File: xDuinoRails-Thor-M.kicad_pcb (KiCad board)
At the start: 6 copper layers, 30 x 20.1 mm, 38 parts, among them J701 Conn_02x11_Odd_Even, Q501 S8050, Q601 S8550, Q602 S8550, Q604 S8050, Q901 BSS138, Q902 BSS138, U1101 MOUDLE-SEEEDUINO-XIAO, U201 HT75xx-1-SOT89, U801 BDR6133

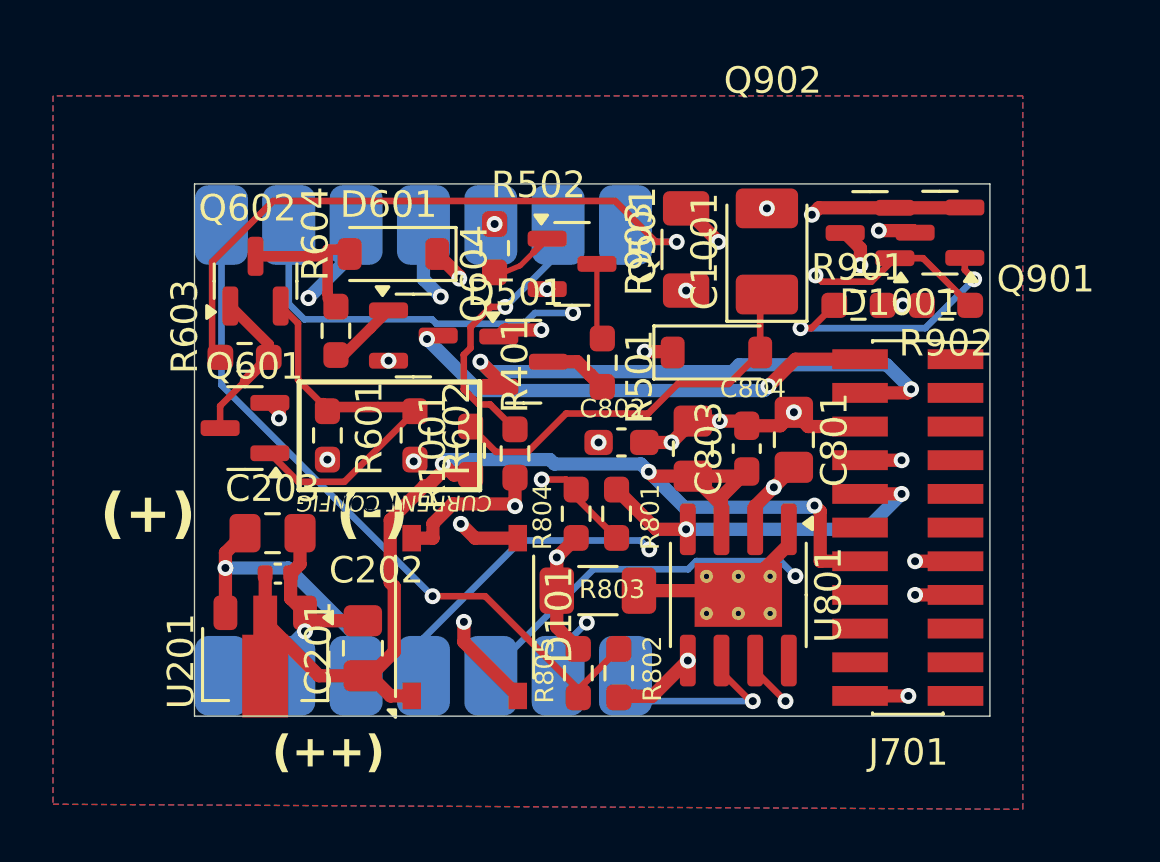
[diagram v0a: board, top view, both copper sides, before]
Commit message: Chg - Clearer PCB layout
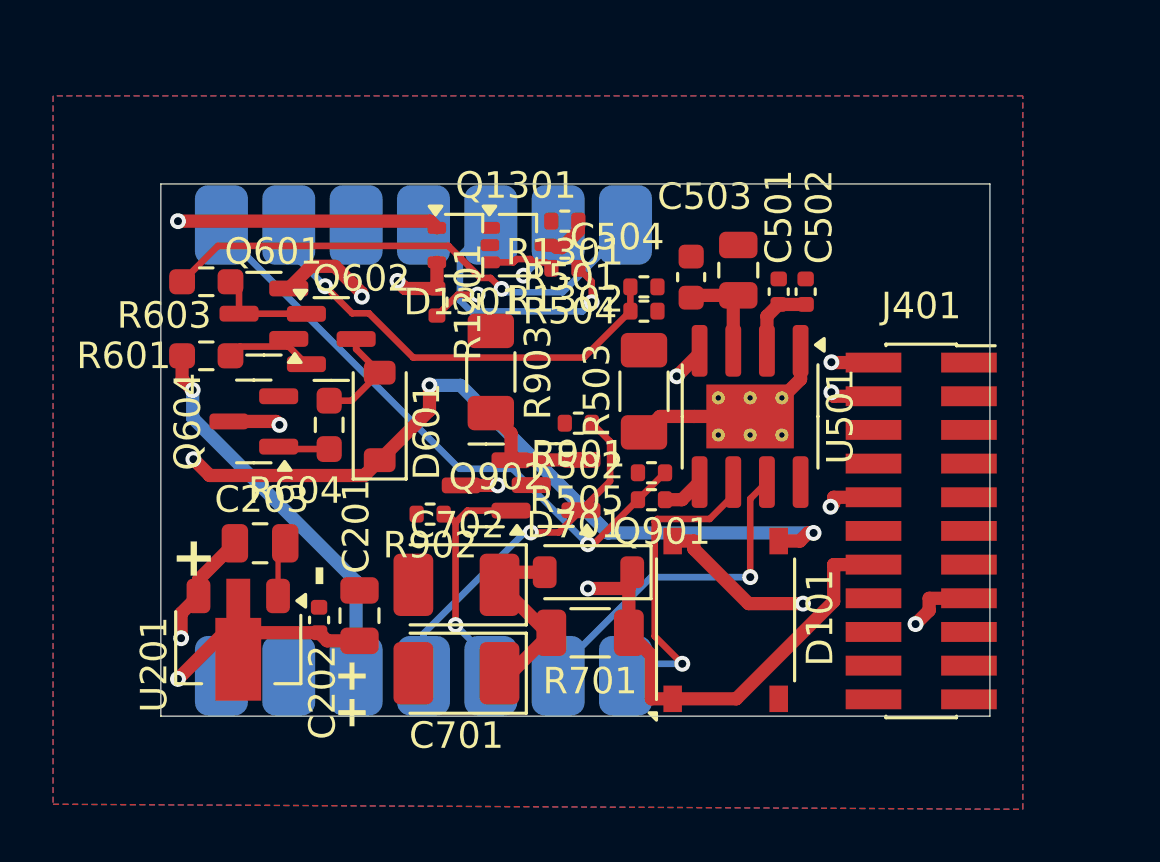
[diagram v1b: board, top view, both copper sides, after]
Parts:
- removed C1001: 100uF, Capacitor_Tantalum_SMD:CP_EIA-3528-21_Kemet-B_Pad1.50x2.35mm_HandSolder
- removed C801, C804: 100nF, Capacitor_SMD:C_0805_2012Metric_Pad1.18x1.45mm_HandSolder
- removed C802, C803: 10uF, Capacitor_SMD:C_0603_1608Metric_Pad1.08x0.95mm_HandSolder
- removed D1001: 1N5819W, Diode_SMD:D_SOD-123
- removed D501: BAT54C, xDuinoRail:8x50_SOT-23
- removed J701: Conn_02x11_Odd_Even, Connector_PinSocket_1.27mm:PinSocket_2x11_P1.27mm_Vertical_SMD
- removed Q501: S8050, xDuinoRail:8x50_SOT-23
- removed R1001: 100R, Resistor_SMD:R_0603_1608Metric_Pad0.98x0.95mm_HandSolder
- removed R401: 33k, Resistor_SMD:R_0603_1608Metric_Pad0.98x0.95mm_HandSolder
- removed R602: 1M, Resistor_SMD:R_0603_1608Metric_Pad0.98x0.95mm_HandSolder
- removed R801, R802: 6k8, Resistor_SMD:R_0603_1608Metric_Pad0.98x0.95mm_HandSolder
- removed R803: 0R1, Resistor_SMD:R_1206_3216Metric_Pad1.30x1.75mm_HandSolder
- removed R804, R805: 1k, Resistor_SMD:R_0603_1608Metric_Pad0.98x0.95mm_HandSolder
- removed U801: BDR6133, Package_SO:SOIC-8-1EP_3.9x4.9mm_P1.27mm_EP2.41x3.3mm_ThermalVias
- added C501: 100nF, Capacitor_SMD:C_0402_1005Metric, F.Cu at (165.0, 93.5)
- added C502: 10uF, Capacitor_SMD:C_0402_1005Metric, F.Cu at (166.1, 93.5)
- added C503: 10uF, Capacitor_SMD:C_0805_2012Metric, F.Cu at (163.5, 92.7)
- added C504: 100nF, Capacitor_SMD:C_0603_1608Metric, F.Cu at (161.7, 92.9)
- added C701: 100uF, Capacitor_Tantalum_SMD:CP_EIA-3528-21_Kemet-B_Pad1.50x2.35mm_HandSolder, F.Cu at (152.9, 107.9)
- added C702: 100uF, Capacitor_Tantalum_SMD:CP_EIA-3528-21_Kemet-B_Pad1.50x2.35mm_HandSolder, F.Cu at (152.9, 104.5)
- added D1301: BAT54CW, Package_TO_SOT_SMD:SOT-323_SC-70, F.Cu at (153.1, 91.7)
- added D701: 1N5819W, Diode_SMD:D_SOD-123, F.Cu at (157.9, 104.0)
- added J401: Conn_02x11_Odd_Even, Connector_PinSocket_1.27mm:PinSocket_2x11_P1.27mm_Vertical_SMD, F.Cu at (170.4, 102.5)
- added Q1301: BSS138W, Package_TO_SOT_SMD:SOT-323_SC-70, F.Cu at (155.2, 91.7)
- added R1201: 33k, Resistor_SMD:R_0402_1005Metric, F.Cu at (152.1, 93.9)
- added R1301: 100R, Resistor_SMD:R_0402_1005Metric, F.Cu at (157.0, 90.8)
- added R1302: 10k, Resistor_SMD:R_0402_1005Metric, F.Cu at (157.0, 92.6)
- added R503: 0R1, Resistor_SMD:R_1206_3216Metric_Pad1.30x1.75mm_HandSolder, F.Cu at (160.0, 97.2)
- added R504: 1k, Resistor_SMD:R_0402_1005Metric, F.Cu at (160.0, 94.2)
- added R505: 1k, Resistor_SMD:R_0402_1005Metric, F.Cu at (160.2, 100.3)
- added R701: 100R, Resistor_SMD:R_1206_3216Metric, F.Cu at (157.9, 106.3)
- added U501: BDR6133, Package_SO:SOIC-8-1EP_3.9x4.9mm_P1.27mm_EP2.41x3.3mm_ThermalVias, F.Cu at (164.0, 98.2)
- C201, C203: footprint Capacitor_SMD:C_0805_2012Metric_Pad1.18x1.45mm_HandSolder -> Capacitor_SMD:C_0805_2012Metric
- R501: value 100R -> 6k8; footprint Resistor_SMD:R_0603_1608Metric_Pad0.98x0.95mm_HandSolder -> Resistor_SMD:R_0402_1005Metric
- R502: value 10k -> 6k8; footprint Resistor_SMD:R_0603_1608Metric_Pad0.98x0.95mm_HandSolder -> Resistor_SMD:R_0402_1005Metric
- R901, R902: footprint Resistor_SMD:R_0603_1608Metric_Pad0.98x0.95mm_HandSolder -> Resistor_SMD:R_0402_1005Metric
- moved R902 21.0 mm to (151.9, 101.9)
- moved Q902 17.3 mm to (154.0, 100.8)
- moved Q901 17.3 mm to (156.6, 100.8)
- moved R901 11.5 mm to (157.5, 98.4), turned to 180 degrees
- moved R502 11.2 mm to (160.2, 101.3), turned to 0 degrees
- moved D101 9.84 mm to (163.0, 105.8)
- moved R903 8.70 mm to (154.2, 96.5), turned to -90 degrees
- moved Q604 6.83 mm to (145.2, 98.4), turned to 180 degrees
- moved D601 6.15 mm to (150.0, 98.2), turned to 90 degrees
- moved R601 5.47 mm to (143.4, 95.9), turned to 180 degrees
- moved Q601 4.37 mm to (145.6, 94.3)
- moved Q602 3.59 mm to (148.2, 95.2), turned to 0 degrees
- moved R604 3.56 mm to (148.1, 98.5)
- moved R501 3.26 mm to (160.0, 93.3), turned to 0 degrees
- moved R603 3.20 mm to (143.4, 93.1)
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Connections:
- R501 pad 1: /rails_signal_combined-medium/rails-signal-acknowledge_dcc/DCC+_DROP -> /EMF_MOTOR0
- R501 pad 2: /rails_signal_combined-medium/rails-signal-acknowledge_dcc/DCC+ -> /AMP_MOTOR0
- R502 pad 1: /DCC_ACK -> /EMF_MOTOR1
- R502 pad 2: /rails_signal_combined-medium/rails-signal-acknowledge_dcc/DCC_ACK_IN -> /AMP_MOTOR1
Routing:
- net GND: track 27.2 -> 1.71 mm, vias 11 -> 0
- net /FUNC1: track 32.8 -> 9.19 mm, vias 2 -> 1
- net PGND: track 36.0 -> 13.9 mm, vias 1 -> 0
- net /I_FUNC: track 26.6 -> 4.73 mm, vias 3 -> 0
- net /AMP_MOTOR1: track 21.5 -> 1.58 mm, vias 2 -> 0
- net /FUNC0: track 32.2 -> 13.5 mm, vias 3 -> 1
- net /AMP_FUNC0: track 16.0 -> 0.00 mm, vias 2 -> 0
- net /DCC0: track 40.7 -> 56.4 mm, vias 4 -> 5
- net Net-(D1001-A): track 15.2 -> 0.00 mm
- net /rails_signal_combined-medium/rails_signal_feedback_dcc-railcom-8x50/RC_CURR: track 16.7 -> 3.57 mm
- net /DCC1: track 36.6 -> 49.7 mm
- net /DCC_ACK: track 0.16 -> 10.1 mm
- net /+3V3: track 16.5 -> 25.8 mm, vias 7 -> 3
- net /EMF_MOTOR0: track 24.9 -> 17.1 mm, vias 2 -> 1
- net /rails_power-buffer/BUFF_U+: track 0.00 -> 7.19 mm
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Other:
- board size 30 x 20.1 mm -> 31.3 x 20.1 mm
- board text added: "+"
- board text added: "++"
- board text added: "-"
- board text removed: "(+)"
- board text removed: "(++)"
- board text removed: "(-)"
- board text removed: "CURRENT CONFIG"
